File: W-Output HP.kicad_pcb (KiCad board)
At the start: 4 copper layers, 50 x 50 mm, 95 parts, among them J1 Conn_01x10, J2 Conn_01x08, J3 Conn_01x03, J4 NC3MBH-1, J5 NC3MBH-1, K1 G6K-2, K2 G6K-2, Q1 MMBT3906, Q2 MMBT3904, Q3 MMBT3904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

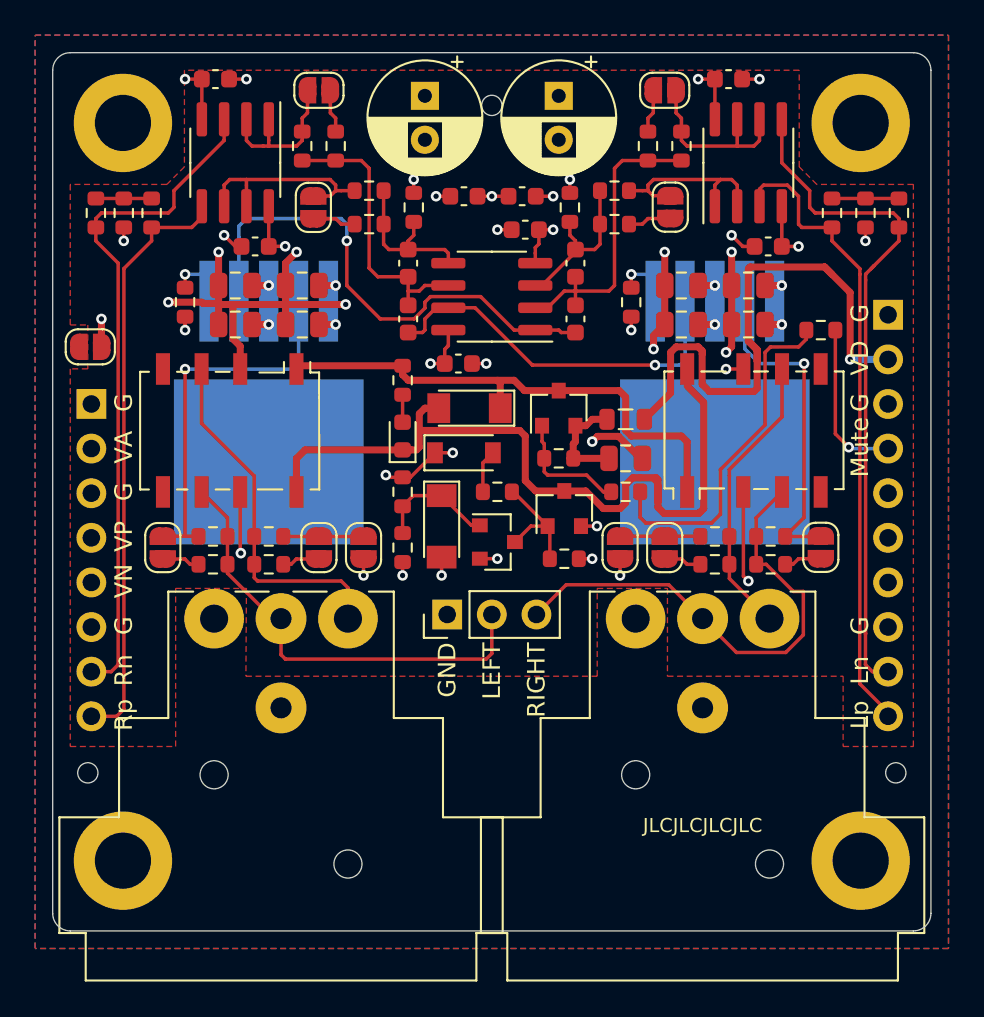
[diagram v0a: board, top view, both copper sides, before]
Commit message: Add missing feedback resistor
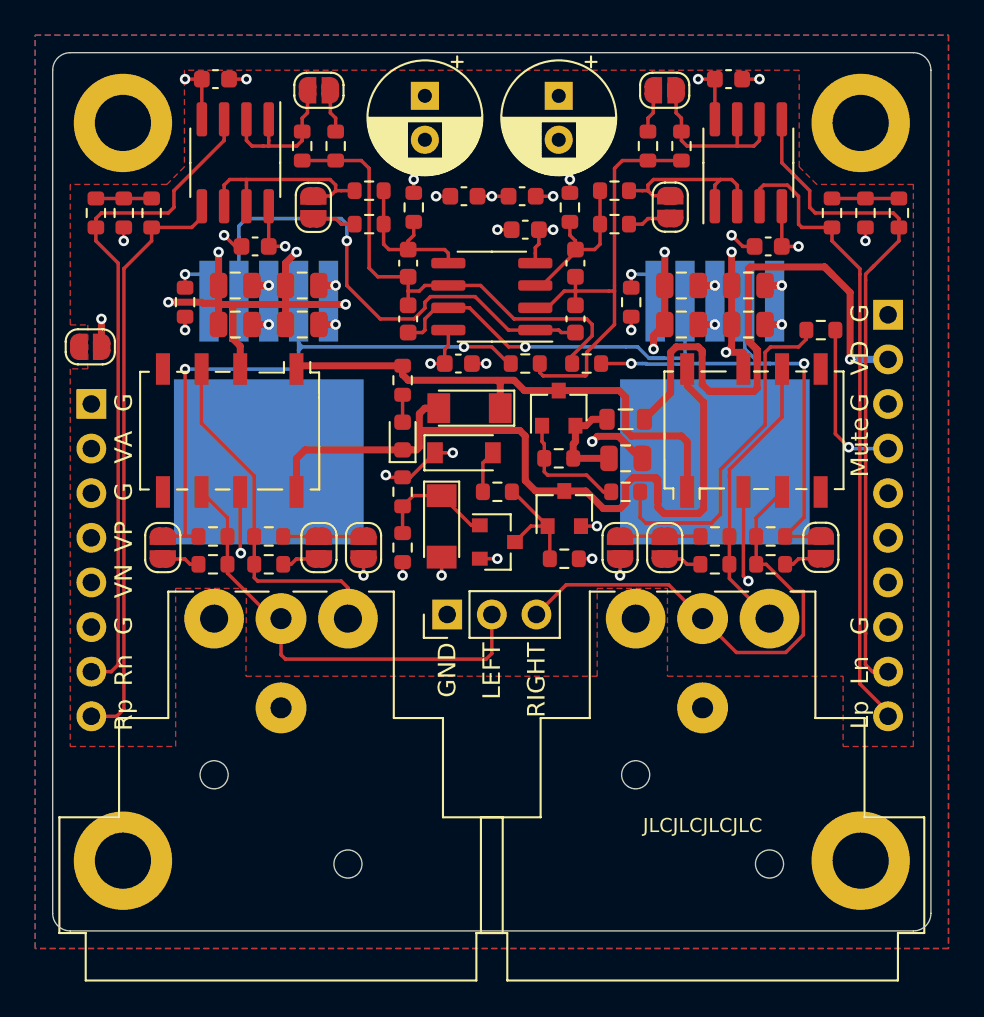
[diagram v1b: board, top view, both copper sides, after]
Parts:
- removed REF** (x3): MountingHole_JLCPCB, MountingHole:MountingHole_JLCPCB
- added R35: 1k, Resistor_SMD:R_0603_1608Metric, F.Cu at (151.9, 92.7)
- added R36: 1k, Resistor_SMD:R_0603_1608Metric, F.Cu at (155.4, 92.7)
- J3: value Conn_01x03 -> OUT
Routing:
- net Net-(JP2-Pad1): track 22.3 -> 35.1 mm, vias 1 -> 2
- net Net-(C17-Pad1): track 16.1 -> 27.9 mm
- net Net-(JP7-Pad1): track 18.8 -> 28.8 mm, vias 1 -> 2
- net Net-(C4-Pad1): track 17.3 -> 26.2 mm
- net GND: track 67.0 -> 67.9 mm, vias 30 -> 29
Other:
- net class Default removed
- board text added: "W-Output HP Rev. 2, 2021-03-27 Tobias Müller, twam.info"
- board text removed: "W-Output HP Rev. 1, 2021-03-06 Tobias Müller, twam.info"
